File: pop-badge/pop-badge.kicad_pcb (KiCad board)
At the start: 2 copper layers, 129.5 x 101.3 mm, 164 parts, among them J1 Conn_01x05, Q1 S9013, Q2 AO3400A, U1 WS2812-2020, U10 WS2812-2020, U11 WS2812-2020, U12 WS2812-2020, U13 WS2812-2020, U14 WS2812-2020, U15 WS2812-2020, U16 WS2812-2020, U17 WS2812-2020, U18 WS2812-2020, U19 WS2812-2020, U2 WS2812-2020, U20 WS2812-2020, U21 WS2812-2020, U22 WS2812-2020, U23 WS2812-2020, U24 WS2812-2020, U25 WS2812-2020, U26 Pico, U3 WS2812-2020, U4 WS2812-2020, U5 WS2812-2020, U6 WS2812-2020, U7 WS2812-2020, U8 WS2812-2020, U9 WS2812-2020

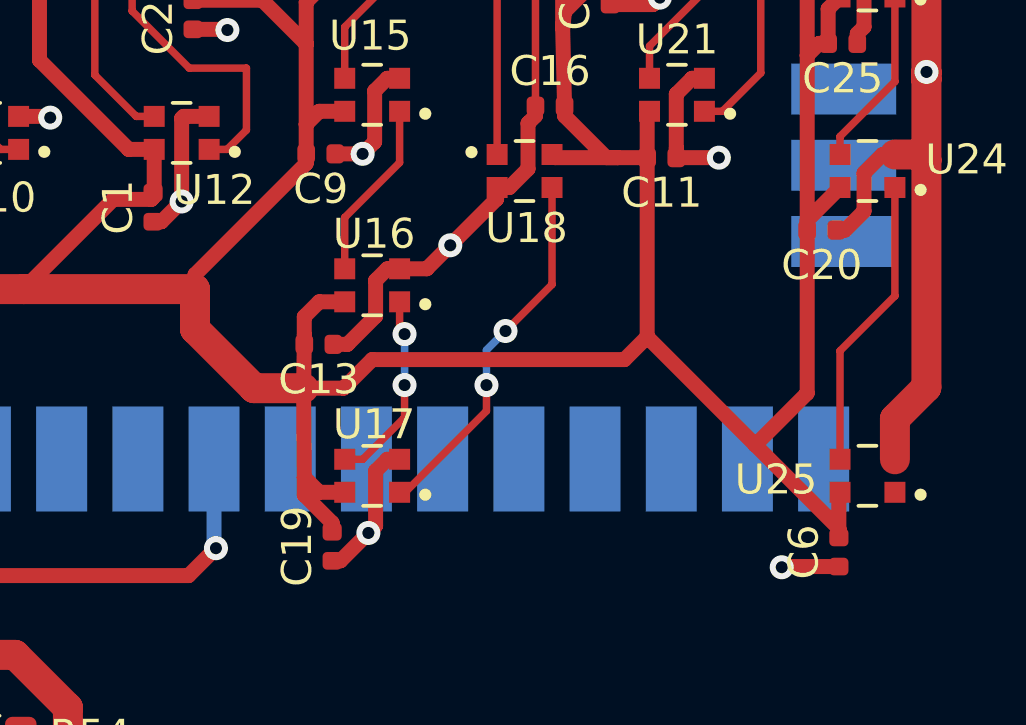
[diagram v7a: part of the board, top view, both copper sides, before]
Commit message: slight tracking changes
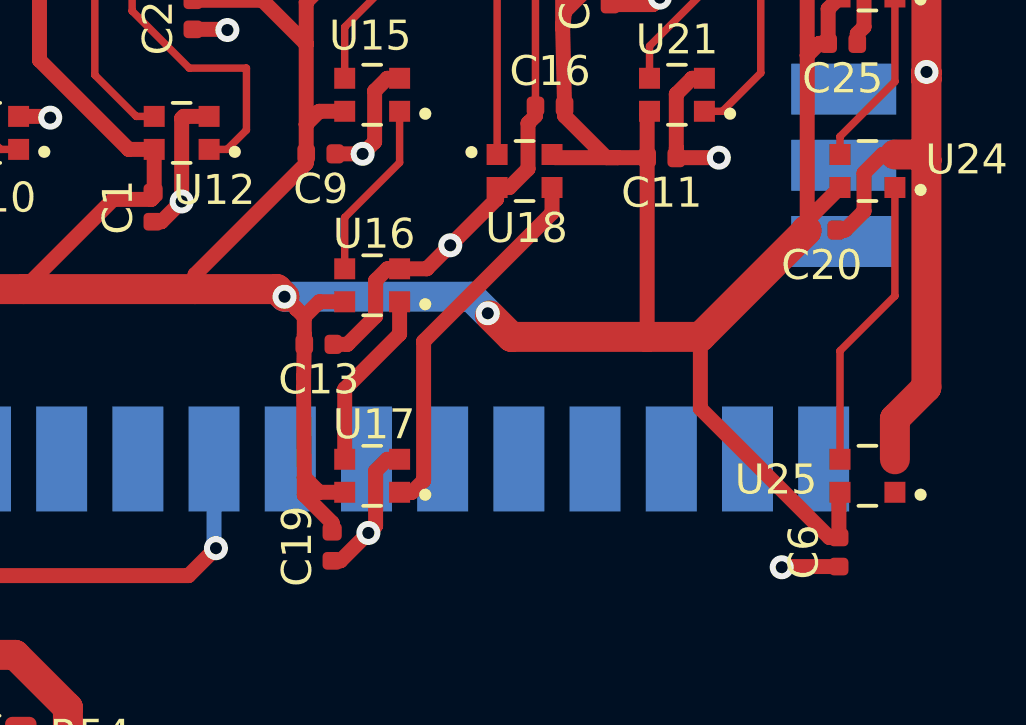
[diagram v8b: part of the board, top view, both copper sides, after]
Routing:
- net +5V: track 645.3 -> 642.3 mm, vias 1 -> 3
- net Net-(U16-Pad1): track 6.67 -> 6.01 mm, vias 2 -> 0
- net Net-(U17-Pad1): vias 2 -> 0
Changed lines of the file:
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@@
     (thickness 1.6)
     (drawings 25)
-    (tracks 745)
+    (tracks 740)
     (zones 0)
     (modules 164)
@@
   (page A4)
   (layers
-    (0 F.Cu signal hide)
-    (31 B.Cu signal hide)
-    (32 B.Adhes user hide)
-    (33 F.Adhes user hide)
-    (34 B.Paste user hide)
+    (0 F.Cu signal)
+    (31 B.Cu signal)
+    (32 B.Adhes user)
+    (33 F.Adhes user)
+    (34 B.Paste user)
     (35 F.Paste user)
-    (36 B.SilkS user hide)
+    (36 B.SilkS user)
     (37 F.SilkS user)
-    (38 B.Mask user hide)
+    (38 B.Mask user)
     (39 F.Mask user)
-    (40 Dwgs.User user hide)
-    (41 Cmts.User user hide)
-    (42 Eco1.User user hide)
-    (43 Eco2.User user hide)
-    (44 Edge.Cuts user hide)
-    (45 Margin user hide)
-    (46 B.CrtYd user hide)
-    (47 F.CrtYd user hide)
-    (48 B.Fab user hide)
+    (40 Dwgs.User user)
+    (41 Cmts.User user)
+    (42 Eco1.User user)
+    (43 Eco2.User user)
+    (44 Edge.Cuts user)
+    (45 Margin user)
+    (46 B.CrtYd user)
+    (47 F.CrtYd user)
+    (48 B.Fab user)
     (49 F.Fab user hide)
   )
   (setup
-    (last_trace_width 1)
+    (last_trace_width 0.5)
     (user_trace_width 0.25)
     (user_trace_width 0.5)
@@
   (segment (start 74.396 94.514) (end 74.396 96.224) (width 0.25) (layer F.Cu) (net 69) (status 20))
   (segment (start 76.226 92.684) (end 74.396 94.514) (width 0.25) (layer F.Cu) (net 69))
-  (segment (start 76.3905 101.1795) (end 76.3905 100.1005) (width 0.25) (layer F.Cu) (net 70))
-  (via (at 76.3905 100.1005) (size 0.8) (drill 0.4) (layers F.Cu B.Cu) (net 70))
-  (segment (start 74.996 102.574) (end 76.3905 101.1795) (width 0.25) (layer F.Cu) (net 70))
-  (segment (start 74.396 102.574) (end 74.996 102.574) (width 0.25) (layer F.Cu) (net 70) (status 10))
-  (segment (start 76.3905 100.1005) (end 76.3905 98.4005) (width 0.25) (layer B.Cu) (net 70))
-  (via (at 76.3905 98.4005) (size 0.8) (drill 0.4) (layers F.Cu B.Cu) (net 70))
-  (segment (start 76.3905 98.4005) (end 76.3905 98.4885) (width 0.25) (layer F.Cu) (net 70))
-  (segment (start 76.226 98.324) (end 76.226 97.324) (width 0.25) (layer F.Cu) (net 70) (status 20))
-  (segment (start 76.3905 98.4885) (end 76.226 98.324) (width 0.25) (layer F.Cu) (net 70))
-  (segment (start 76.226 103.674) (end 76.226 103.733) (width 0.25) (layer F.Cu) (net 71) (status 30))
-  (via (at 79.121 100.1005) (size 0.8) (drill 0.4) (layers F.Cu B.Cu) (net 71))
-  (segment (start 79.121 100.964002) (end 79.121 100.1005) (width 0.25) (layer F.Cu) (net 71))
-  (segment (start 76.352002 103.733) (end 79.121 100.964002) (width 0.25) (layer F.Cu) (net 71) (status 10))
-  (segment (start 76.226 103.733) (end 76.352002 103.733) (width 0.25) (layer F.Cu) (net 71) (status 30))
-  (via (at 79.756 98.298) (size 0.8) (drill 0.4) (layers F.Cu B.Cu) (net 71))
-  (segment (start 79.121 98.933) (end 79.756 98.298) (width 0.25) (layer B.Cu) (net 71))
-  (segment (start 79.121 100.1005) (end 79.121 98.933) (width 0.25) (layer B.Cu) (net 71))
-  (segment (start 81.306 96.748) (end 81.306 93.514) (width 0.25) (layer F.Cu) (net 71) (status 20))
-  (segment (start 79.756 98.298) (end 81.306 96.748) (width 0.25) (layer F.Cu) (net 71))
+  (segment (start 74.396 102.574) (end 74.396 100.229) (width 0.5) (layer F.Cu) (net 70))
+  (segment (start 76.226 98.399) (end 76.226 97.324) (width 0.5) (layer F.Cu) (net 70))
+  (segment (start 74.396 100.229) (end 76.226 98.399) (width 0.5) (layer F.Cu) (net 70))
+  (segment (start 81.306 94.364) (end 81.306 93.514) (width 0.5) (layer F.Cu) (net 71))
+  (segment (start 77.026001 98.643999) (end 81.306 94.364) (width 0.5) (layer F.Cu) (net 71))
+  (segment (start 77.026001 103.284001) (end 77.026001 98.643999) (width 0.5) (layer F.Cu) (net 71))
+  (segment (start 76.636002 103.674) (end 77.026001 103.284001) (width 0.5) (layer F.Cu) (net 71))
+  (segment (start 76.226 103.674) (end 76.636002 103.674) (width 0.5) (layer F.Cu) (net 71))
   (segment (start 78.876 80.984) (end 79.476 80.984) (width 0.25) (layer F.Cu) (net 72) (status 20))
   (segment (start 77.47 82.39) (end 78.876 80.984) (width 0.25) (layer F.Cu) (net 72))
@@
   (segment (start 90.8685 105.179) (end 90.8685 103.7115) (width 0.5) (layer F.Cu) (net 80) (status 30))
   (segment (start 84.478 98.4935) (end 84.478 92.5195) (width 0.5) (layer F.Cu) (net 80) (status 20))
-  (segment (start 90.8685 105.179) (end 90.8685 104.884) (width 0.5) (layer F.Cu) (net 80) (status 30))
   (segment (start 84.478 91.052) (end 84.556 90.974) (width 0.5) (layer F.Cu) (net 80) (status 30))
   (segment (start 84.478 92.5195) (end 84.478 91.052) (width 0.5) (layer F.Cu) (net 80) (status 30))
@@
   (segment (start 84.478 92.5195) (end 83.5025 92.5195) (width 0.5) (layer F.Cu) (net 80) (status 10))
   (segment (start 83.5025 92.5195) (end 81.4115 92.5195) (width 0.5) (layer F.Cu) (net 80) (status 20))
-  (segment (start 89.812 100.3705) (end 89.812 94.9325) (width 0.5) (layer F.Cu) (net 80) (status 20))
-  (segment (start 88.0835 102.099) (end 89.812 100.3705) (width 0.5) (layer F.Cu) (net 80))
-  (segment (start 90.8685 104.884) (end 88.0835 102.099) (width 0.5) (layer F.Cu) (net 80) (status 10))
-  (segment (start 88.0835 102.099) (end 84.478 98.4935) (width 0.5) (layer F.Cu) (net 80))
   (segment (start 89.812 94.608) (end 89.812 94.9325) (width 0.5) (layer F.Cu) (net 80) (status 20))
   (segment (start 90.906 93.514) (end 89.812 94.608) (width 0.5) (layer F.Cu) (net 80) (status 10))
@@
   (segment (start 44.6405 110.363) (end 44.577 110.4265) (width 1) (layer B.Cu) (net 80) (status 30))
   (segment (start 44.6405 101.6635) (end 44.6405 110.363) (width 1) (layer B.Cu) (net 80) (status 30))
-  (segment (start 69.4055 96.901) (end 69.4055 98.2345) (width 1) (layer F.Cu) (net 80))
-  (segment (start 71.374 100.203) (end 73.025 100.203) (width 1) (layer F.Cu) (net 80))
-  (segment (start 69.4055 98.2345) (end 71.374 100.203) (width 1) (layer F.Cu) (net 80))
   (segment (start 73.025 100.203) (end 73.048 103.176) (width 0.5) (layer F.Cu) (net 80))
-  (segment (start 73.048 98.7425) (end 73.025 100.203) (width 0.5) (layer F.Cu) (net 80) (status 10))
-  (segment (start 73.025 100.203) (end 74.3585 100.203) (width 0.5) (layer F.Cu) (net 80))
-  (segment (start 74.3585 100.203) (end 75.311 99.2505) (width 0.5) (layer F.Cu) (net 80))
-  (segment (start 83.721 99.2505) (end 84.478 98.4935) (width 0.5) (layer F.Cu) (net 80))
-  (segment (start 75.311 99.2505) (end 83.721 99.2505) (width 0.5) (layer F.Cu) (net 80))
   (segment (start 50.198 120.791) (end 50.673 120.791) (width 1) (layer F.Cu) (net 80) (status 30))
   (segment (start 49.3775 120.791) (end 50.198 120.791) (width 1) (layer F.Cu) (net 80) (status 20))
@@
   (segment (start 44.704 120.777) (end 50.198 120.791) (width 1) (layer F.Cu) (net 80) (status 20))
   (segment (start 43.274 120.791) (end 44.704 120.777) (width 1) (layer F.Cu) (net 80))
+  (segment (start 73.025 99.822) (end 73.025 100.203) (width 0.5) (layer F.Cu) (net 80))
+  (segment (start 73.048 98.7425) (end 73.025 99.822) (width 0.5) (layer F.Cu) (net 80))
+  (segment (start 89.78699 94.95751) (end 89.78699 94.9325) (width 1) (layer F.Cu) (net 80))
+  (segment (start 86.251 98.4935) (end 89.78699 94.95751) (width 1) (layer F.Cu) (net 80))
+  (segment (start 84.478 98.4935) (end 86.251 98.4935) (width 1) (layer F.Cu) (net 80))
+  (segment (start 86.251 100.8815) (end 90.5485 105.179) (width 0.5) (layer F.Cu) (net 80))
+  (segment (start 90.5485 105.179) (end 90.8685 105.179) (width 0.5) (layer F.Cu) (net 80))
+  (segment (start 86.251 98.4935) (end 86.251 100.8815) (width 0.5) (layer F.Cu) (net 80))
+  (segment (start 72.39 97.155) (end 78.613 97.155) (width 1) (layer B.Cu) (net 80))
+  (segment (start 78.613 97.155) (end 79.165041 97.707041) (width 1) (layer B.Cu) (net 80))
+  (segment (start 72.136 96.901) (end 72.39 97.155) (width 1) (layer F.Cu) (net 80))
+  (via (at 79.165041 97.707041) (size 0.8) (drill 0.4) (layers F.Cu B.Cu) (net 80))
+  (segment (start 69.4055 96.901) (end 72.136 96.901) (width 1) (layer F.Cu) (net 80))
+  (via (at 72.39 97.155) (size 0.8) (drill 0.4) (layers F.Cu B.Cu) (net 80))
+  (segment (start 79.9515 98.4935) (end 79.235758 97.777758) (width 1) (layer F.Cu) (net 80))
+  (segment (start 84.478 98.4935) (end 79.9515 98.4935) (width 1) (layer F.Cu) (net 80))
+  (segment (start 72.789999 97.563999) (end 73.048 97.822) (width 0.5) (layer F.Cu) (net 80))
+  (segment (start 72.789999 97.554999) (end 72.789999 97.563999) (width 0.5) (layer F.Cu) (net 80))
+  (segment (start 72.39 97.155) (end 72.789999 97.554999) (width 0.5) (layer F.Cu) (net 80))
   (segment (start 52.211 116.7625) (end 52.197 116.7765) (width 0.5) (layer F.Cu) (net 81) (status 30))
   (via (at 70.104 105.537) (size 0.8) (drill 0.4) (layers F.Cu B.Cu) (net 81))
